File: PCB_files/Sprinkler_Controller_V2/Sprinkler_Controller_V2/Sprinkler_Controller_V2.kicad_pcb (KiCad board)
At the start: 2 copper layers, 116 x 72 mm, 43 parts, among them J1 Screw_Terminal_01x02, J2 Screw_Terminal_01x11, SW1 SW_SPST, U1 ESP32_DevKit_V1_DOIT, U12 TPP362081-T6TR

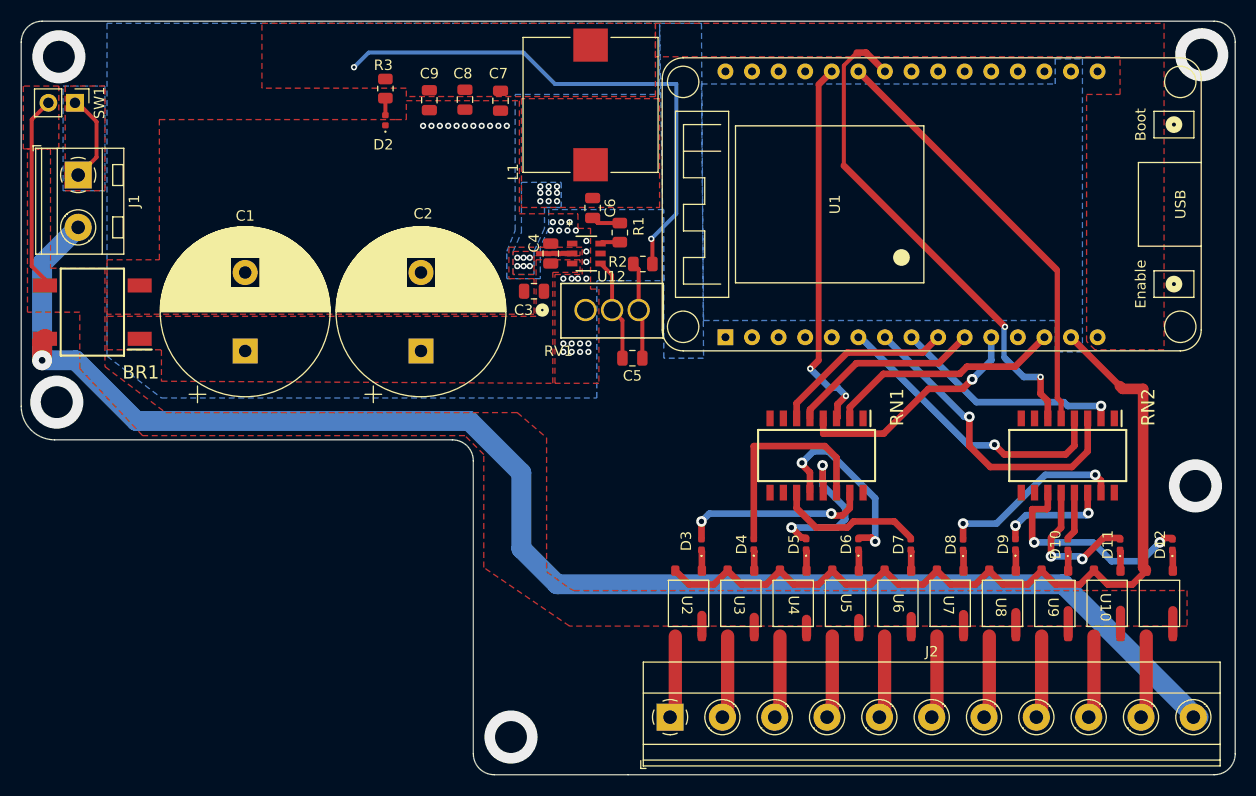
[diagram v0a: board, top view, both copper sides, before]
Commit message: updated size of leds on pcb
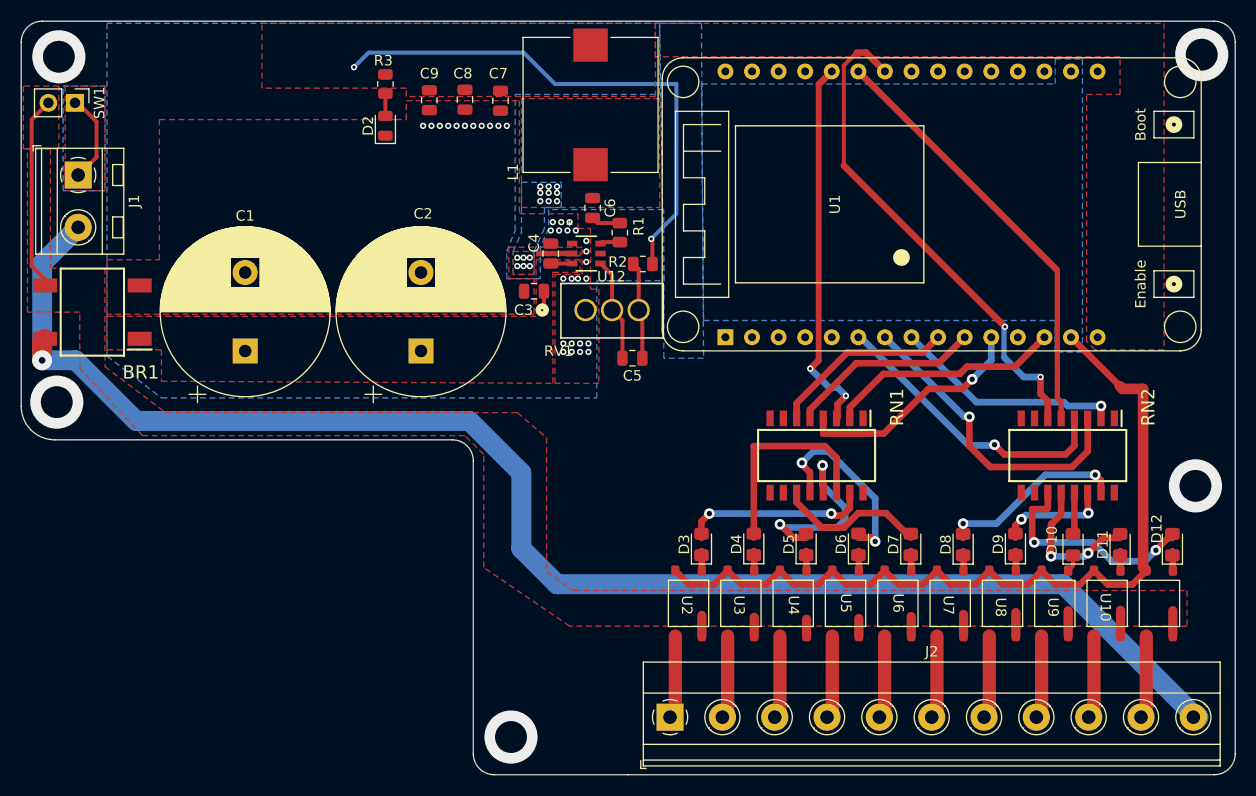
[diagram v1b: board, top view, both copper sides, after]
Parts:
- D10, D11, D12, D3, D4, D5, D6, D7, D8, D9: footprint LED_SMD:LED_0402_1005Metric -> LED_SMD:LED_0805_2012Metric_Pad1.15x1.40mm_HandSolder
- D2: footprint LED_SMD:LED_0402_1005Metric -> LED_SMD:LED_0805_2012Metric
- moved D2 0.53 mm to (131.8, 90.0)
- moved D10 0.50 mm to (197.5, 130.0)
- moved R3 0.44 mm to (131.8, 86.0)
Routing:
- net /Vin: track 0.00 -> 3.77 mm
- net Net-(D5-A): track 15.9 -> 18.4 mm
- net Net-(D10-A): track 4.59 -> 4.00 mm

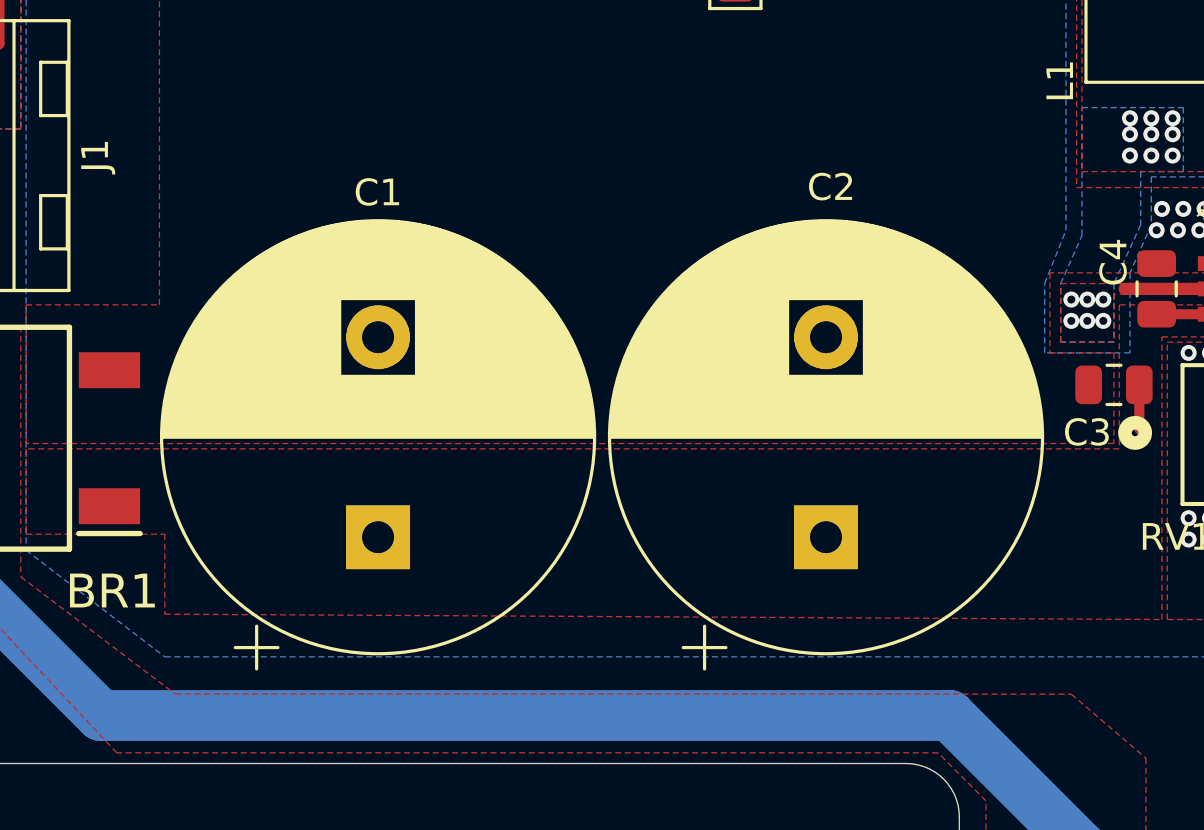
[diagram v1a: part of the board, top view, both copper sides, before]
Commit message: Changed capacitors
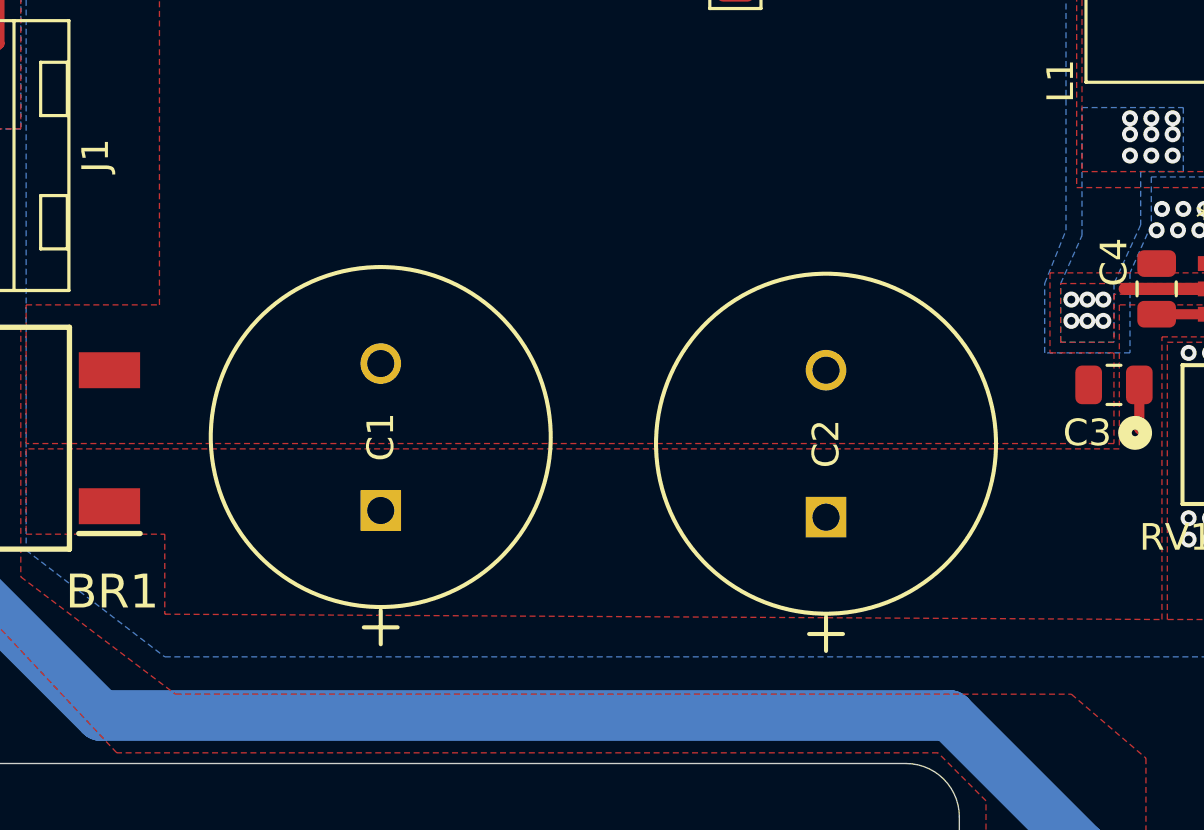
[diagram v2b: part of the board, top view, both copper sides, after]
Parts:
- C1, C2: footprint Capacitor_THT:CP_Radial_D16.0mm_P7.50mm -> footprints:PCAP_12_5x25-THRU-ELECT_NCA
- moved C1 1.01 mm to (118.5, 110.5)
- moved C2 0.75 mm to (135.2, 110.8)
